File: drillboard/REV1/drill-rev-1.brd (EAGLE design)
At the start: 51.4 x 52.6 mm, 41 parts, among them M1 M03VERT, M2 M03VERT, M3 M03VERT, M4 M03VERT, T1 M03VERT, T2 M03VERT, T3 M03VERT, T4 M03VERT

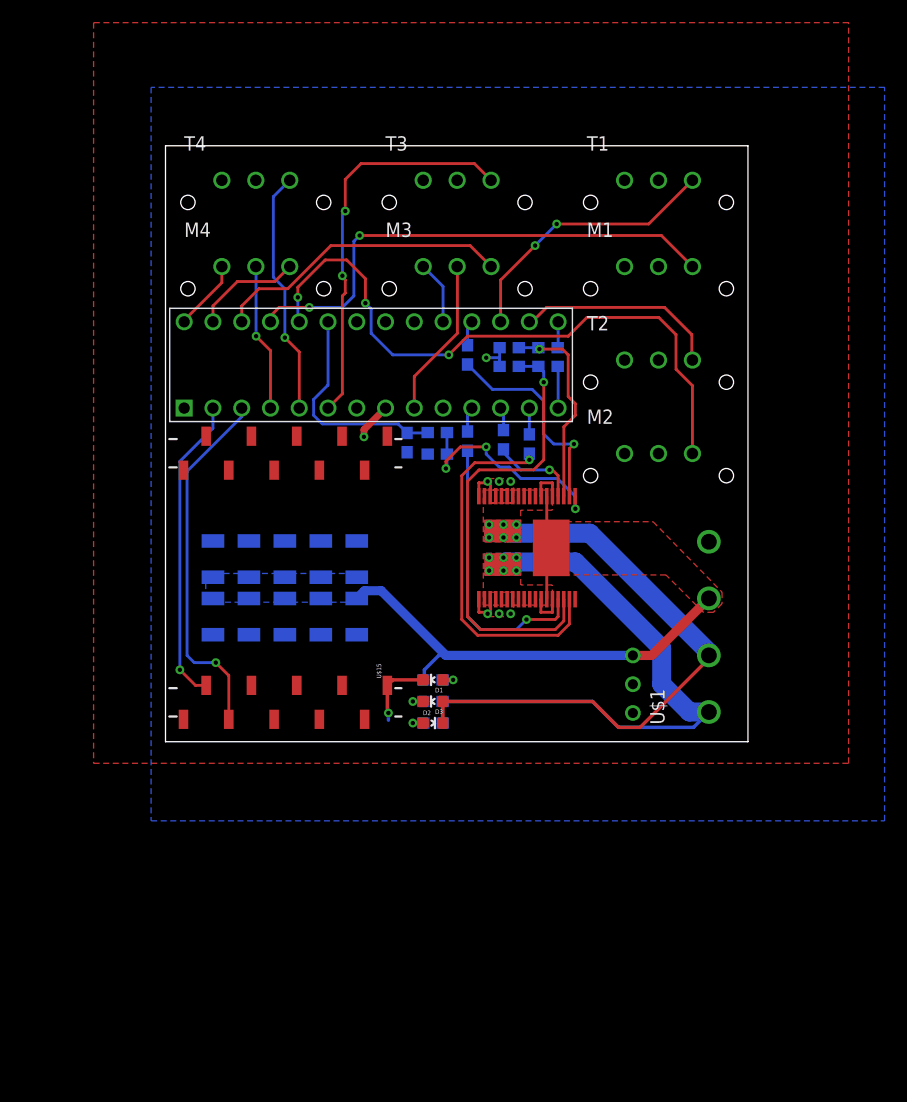
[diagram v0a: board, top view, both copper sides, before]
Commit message: regen gerbers and saved panelized brd file
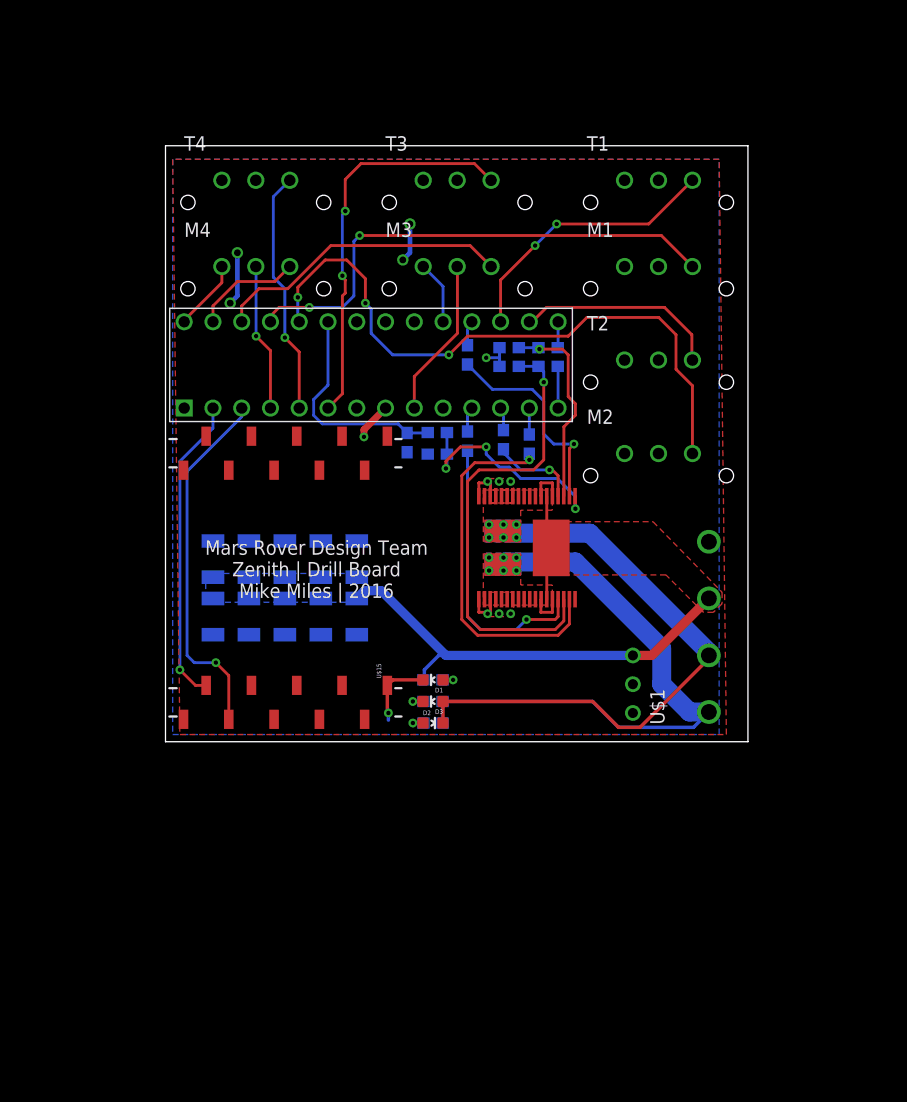
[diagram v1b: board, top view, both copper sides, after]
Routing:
- net +3V3: track 3.57 -> 11.7 mm, vias 1 -> 5
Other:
- board text added: "Mars Rover Design Team Zenith | Drill Board Mike Miles | 2016"
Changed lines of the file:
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@@
 <wire x1="51.435" y1="52.629" x2="0" y2="52.629" width="0" layer="20"/>
 <wire x1="0" y1="52.629" x2="0" y2="0" width="0" layer="20"/>
+<text x="13.335" y="12.7" size="1.27" layer="21" align="bottom-center">Mars Rover Design Team
+Zenith | Drill Board
+Mike Miles | 2016</text>
+<text x="13.335" y="12.7" size="1.27" layer="125" align="bottom-center">Mars Rover Design Team
+Zenith | Drill Board
+Mike Miles | 2016</text>
 </plain>
 <attributes>
@@
 <contactref element="C11" pad="2"/>
 <polygon width="0.4064" layer="16" rank="6">
-<vertex x="-1.27" y="57.785"/>
-<vertex x="-1.27" y="-6.985"/>
-<vertex x="63.5" y="-6.985"/>
-<vertex x="63.5" y="57.785"/>
+<vertex x="0.635" y="51.435"/>
+<vertex x="0.635" y="0.635"/>
+<vertex x="48.895" y="0.635"/>
+<vertex x="48.895" y="51.435"/>
 </polygon>
 <polygon width="0.254" layer="1" thermals="no">
@@
 <contactref element="U$15" pad="14"/>
 <polygon width="0.4064" layer="1" rank="6">
-<vertex x="-6.35" y="63.5"/>
-<vertex x="-6.35" y="-1.905"/>
-<vertex x="60.325" y="-1.905"/>
-<vertex x="60.325" y="63.5"/>
+<vertex x="0.635" y="51.435"/>
+<vertex x="1.27" y="0.635"/>
+<vertex x="49.53" y="0.635"/>
+<vertex x="48.895" y="51.435"/>
 </polygon>
 <wire x1="29.503" y1="34.798" x2="29.503" y2="33.147" width="0.254" layer="16"/>
@@
 <wire x1="29.464" y1="33.909" x2="28.321" y2="33.909" width="0.254" layer="16"/>
 <via x="28.321" y="33.909" extent="1-16" drill="0.381"/>
+<via x="5.715" y="38.735" extent="1-16" drill="0.6"/>
+<via x="6.35" y="43.18" extent="1-16" drill="0.6"/>
+<via x="20.955" y="42.545" extent="1-16" drill="0.6"/>
+<via x="21.59" y="45.72" extent="1-16" drill="0.6"/>
+<wire x1="5.715" y1="38.735" x2="6.35" y2="39.37" width="0.4064" layer="16"/>
+<wire x1="6.35" y1="39.37" x2="6.35" y2="43.18" width="0.4064" layer="16"/>
+<wire x1="20.955" y1="42.545" x2="21.59" y2="43.18" width="0.4064" layer="16"/>
+<wire x1="21.59" y1="43.18" x2="21.59" y2="45.72" width="0.4064" layer="16"/>
 </signal>
 <signal name="+12V">

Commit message: regen gerbers
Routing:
- net GND: track 16.5 -> 23.2 mm, vias 8 -> 10
- net OUTA: track 55.9 -> 58.9 mm
- net OUTB: track 54.6 -> 57.6 mm
- net +3V3: track 11.7 -> 13.7 mm
- net N$5: track 1.83 -> 2.59 mm
- net N$4: track 1.83 -> 2.59 mm
- net N$12: track 1.83 -> 2.59 mm
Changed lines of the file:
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@@
 <setting verticaltext="up"/>
 </settings>
-<grid distance="0.025" unitdist="inch" unit="inch" style="lines" multiple="1" display="yes" altdistance="0.005" altunitdist="inch" altunit="inch"/>
+<grid distance="0.005" unitdist="inch" unit="inch" style="lines" multiple="1" display="yes" altdistance="0.0005" altunitdist="inch" altunit="inch"/>
 <layers>
 <layer number="1" name="Top" color="4" fill="1" visible="yes" active="yes"/>
@@
 <plain>
 <wire x1="0" y1="0" x2="51.435" y2="0" width="0" layer="20"/>
-<wire x1="51.435" y1="0" x2="51.435" y2="52.629" width="0" layer="20"/>
-<wire x1="51.435" y1="52.629" x2="0" y2="52.629" width="0" layer="20"/>
-<wire x1="0" y1="52.629" x2="0" y2="0" width="0" layer="20"/>
+<wire x1="51.435" y1="0" x2="51.435" y2="52.6288" width="0" layer="20"/>
+<wire x1="51.435" y1="52.6288" x2="0" y2="52.6288" width="0" layer="20"/>
+<wire x1="0" y1="52.6288" x2="0" y2="0" width="0" layer="20"/>
 <text x="13.335" y="12.7" size="1.27" layer="21" align="bottom-center">Mars Rover Design Team
 Zenith | Drill Board
@@
 <contactref element="C10" pad="2"/>
 <contactref element="C11" pad="2"/>
-<polygon width="0.4064" layer="16" rank="6">
+<polygon width="0.4064" layer="16" isolate="0.254" rank="6">
 <vertex x="0.635" y="51.435"/>
 <vertex x="0.635" y="0.635"/>
@@
 <vertex x="48.895" y="51.435"/>
 </polygon>
-<polygon width="0.254" layer="1" thermals="no">
+<polygon width="0.254" layer="1" isolate="0.254" thermals="no">
 <vertex x="30.734" y="13.208"/>
 <vertex x="30.734" y="11.049"/>
@@
 <via x="29.464" y="11.303" extent="1-16" drill="0.381"/>
 <via x="30.48" y="11.303" extent="1-16" drill="0.381"/>
-<polygon width="0.254" layer="1" thermals="no">
+<polygon width="0.254" layer="1" isolate="0.254" thermals="no">
 <vertex x="30.734" y="21.082"/>
 <vertex x="30.734" y="23.241"/>
@@
 <wire x1="17.526" y1="26.924" x2="17.526" y2="27.559" width="0.6096" layer="1"/>
 <wire x1="17.526" y1="27.559" x2="19.431" y2="29.464" width="0.6096" layer="1"/>
+<wire x1="41.275" y1="5.08" x2="39.116" y2="5.08" width="0.6096" layer="16"/>
+<wire x1="39.116" y1="5.08" x2="37.973" y2="6.223" width="0.6096" layer="16"/>
+<via x="37.973" y="6.223" extent="1-16" drill="0.381"/>
+<wire x1="37.973" y1="6.223" x2="37.973" y2="9.144" width="0.6096" layer="1"/>
+<via x="37.973" y="9.144" extent="1-16" drill="0.381"/>
 </signal>
 <signal name="+3V3">
@@
 <contactref element="U$15" pad="1"/>
 <contactref element="U$15" pad="14"/>
-<polygon width="0.4064" layer="1" rank="6">
+<polygon width="0.4064" layer="1" isolate="0.254" rank="6">
 <vertex x="0.635" y="51.435"/>
 <vertex x="1.27" y="0.635"/>
@@
 <wire x1="20.955" y1="42.545" x2="21.59" y2="43.18" width="0.4064" layer="16"/>
 <wire x1="21.59" y1="43.18" x2="21.59" y2="45.72" width="0.4064" layer="16"/>
+<wire x1="1.59" y1="1.978" x2="3.556" y2="1.978" width="0.254" layer="1"/>
+<wire x1="3.556" y1="1.978" x2="3.556" y2="2.032" width="0.254" layer="1"/>
 </signal>
 <signal name="+12V">
@@
 <contactref element="U$13" pad="P$3"/>
 <contactref element="U$15" pad="3"/>
-<wire x1="5.59" y1="1.978" x2="5.59" y2="5.84" width="0.254" layer="1"/>
-<wire x1="5.59" y1="5.84" x2="4.445" y2="6.985" width="0.254" layer="1"/>
-<via x="4.445" y="6.985" extent="1-16" drill="0.381"/>
-<wire x1="4.445" y1="6.985" x2="2.54" y2="6.985" width="0.254" layer="16"/>
-<wire x1="2.54" y1="6.985" x2="1.905" y2="7.62" width="0.254" layer="16"/>
-<wire x1="1.905" y1="7.62" x2="1.905" y2="23.876" width="0.254" layer="16"/>
+<wire x1="5.59" y1="1.978" x2="5.59" y2="6.221" width="0.254" layer="1"/>
+<wire x1="5.59" y1="6.221" x2="4.445" y2="7.366" width="0.254" layer="1"/>
+<via x="4.445" y="7.366" extent="1-16" drill="0.381"/>
+<wire x1="4.445" y1="7.366" x2="2.54" y2="7.366" width="0.254" layer="16"/>
+<wire x1="2.54" y1="7.366" x2="1.905" y2="8.001" width="0.254" layer="16"/>
+<wire x1="1.905" y1="8.001" x2="1.905" y2="23.876" width="0.254" layer="16"/>
 <wire x1="1.905" y1="23.876" x2="6.731" y2="28.702" width="0.254" layer="16"/>
 <wire x1="6.731" y1="28.702" x2="6.731" y2="29.464" width="0.254" layer="16"/>
@@
 <contactref element="U$6" pad="P$9"/>
 <contactref element="U$6" pad="P$14"/>
-<polygon width="0.254" layer="1" thermals="no" rank="2">
+<polygon width="0.254" layer="1" isolate="0.254" thermals="no" rank="2">
 <vertex x="34.163" y="12.065"/>
 <vertex x="34.163" y="13.843"/>
@@
 <wire x1="40.005" y1="1.27" x2="46.628" y2="1.27" width="0.3048" layer="16"/>
 <wire x1="46.628" y1="1.27" x2="47.985" y2="2.627" width="0.3048" layer="16"/>
+<wire x1="28.17" y1="12.585" x2="28.1686" y2="12.585" width="0.254" layer="1"/>
+<wire x1="28.1686" y1="12.585" x2="28.1686" y2="14.351" width="0.254" layer="1"/>
+<wire x1="28.1686" y1="14.351" x2="28.575" y2="14.351" width="0.254" layer="1"/>
+<wire x1="28.575" y1="14.351" x2="28.575" y2="15.113" width="0.254" layer="1"/>
 </signal>
 <signal name="OUTB">
@@
 <contactref element="U$6" pad="P$23"/>
 <contactref element="U$6" pad="P$28"/>
-<polygon width="0.254" layer="1" thermals="no">
+<polygon width="0.254" layer="1" isolate="0.254" thermals="no">
 <vertex x="34.163" y="22.225"/>
 <vertex x="34.163" y="20.447"/>
@@
 <wire x1="41.91" y1="1.27" x2="47.985" y2="7.345" width="0.3048" layer="1"/>
 <wire x1="47.985" y1="7.345" x2="47.985" y2="7.627" width="0.3048" layer="1"/>
+<wire x1="28.17" y1="21.685" x2="28.1686" y2="21.685" width="0.254" layer="1"/>
+<wire x1="28.1686" y1="21.685" x2="28.1686" y2="19.7993" width="0.254" layer="1"/>
+<wire x1="28.1686" y1="19.7993" x2="28.575" y2="19.7993" width="0.254" layer="1"/>
+<wire x1="28.575" y1="19.7993" x2="28.575" y2="19.177" width="0.254" layer="1"/>
 </signal>
 <signal name="CS">
@@
 <contactref element="R1" pad="2"/>
 <contactref element="D1" pad="A"/>
-<wire x1="24.499" y1="5.461" x2="25.4" y2="5.461" width="0.254" layer="1"/>
-<via x="25.4" y="5.461" extent="1-16" drill="0.381"/>
-<wire x1="25.4" y1="5.461" x2="24.472" y2="5.461" width="0.254" layer="16"/>
+<wire x1="24.499" y1="5.461" x2="25.781" y2="5.461" width="0.254" layer="1"/>
+<via x="25.781" y="5.461" extent="1-16" drill="0.381"/>
+<wire x1="25.781" y1="5.461" x2="24.472" y2="5.461" width="0.254" layer="16"/>
 </signal>
 <signal name="N$5">
 <contactref element="R12" pad="2"/>
 <contactref element="D2" pad="A"/>
-<wire x1="22.772" y1="1.651" x2="21.844" y2="1.651" width="0.254" layer="16"/>
-<via x="21.844" y="1.651" extent="1-16" drill="0.381"/>
-<wire x1="21.844" y1="1.651" x2="22.745" y2="1.651" width="0.254" layer="1"/>
+<wire x1="22.772" y1="1.651" x2="21.463" y2="1.651" width="0.254" layer="16"/>
+<via x="21.463" y="1.651" extent="1-16" drill="0.381"/>
+<wire x1="21.463" y1="1.651" x2="22.745" y2="1.651" width="0.254" layer="1"/>
 </signal>
 <signal name="N$12">
 <contactref element="D3" pad="C"/>
 <contactref element="R13" pad="2"/>
-<wire x1="22.772" y1="3.556" x2="21.844" y2="3.556" width="0.254" layer="16"/>
-<via x="21.844" y="3.556" extent="1-16" drill="0.381"/>
-<wire x1="21.844" y1="3.556" x2="22.745" y2="3.556" width="0.254" layer="1"/>
+<wire x1="22.772" y1="3.556" x2="21.463" y2="3.556" width="0.254" layer="16"/>
+<via x="21.463" y="3.556" extent="1-16" drill="0.381"/>
+<wire x1="21.463" y1="3.556" x2="22.745" y2="3.556" width="0.254" layer="1"/>
 </signal>
 </signals>

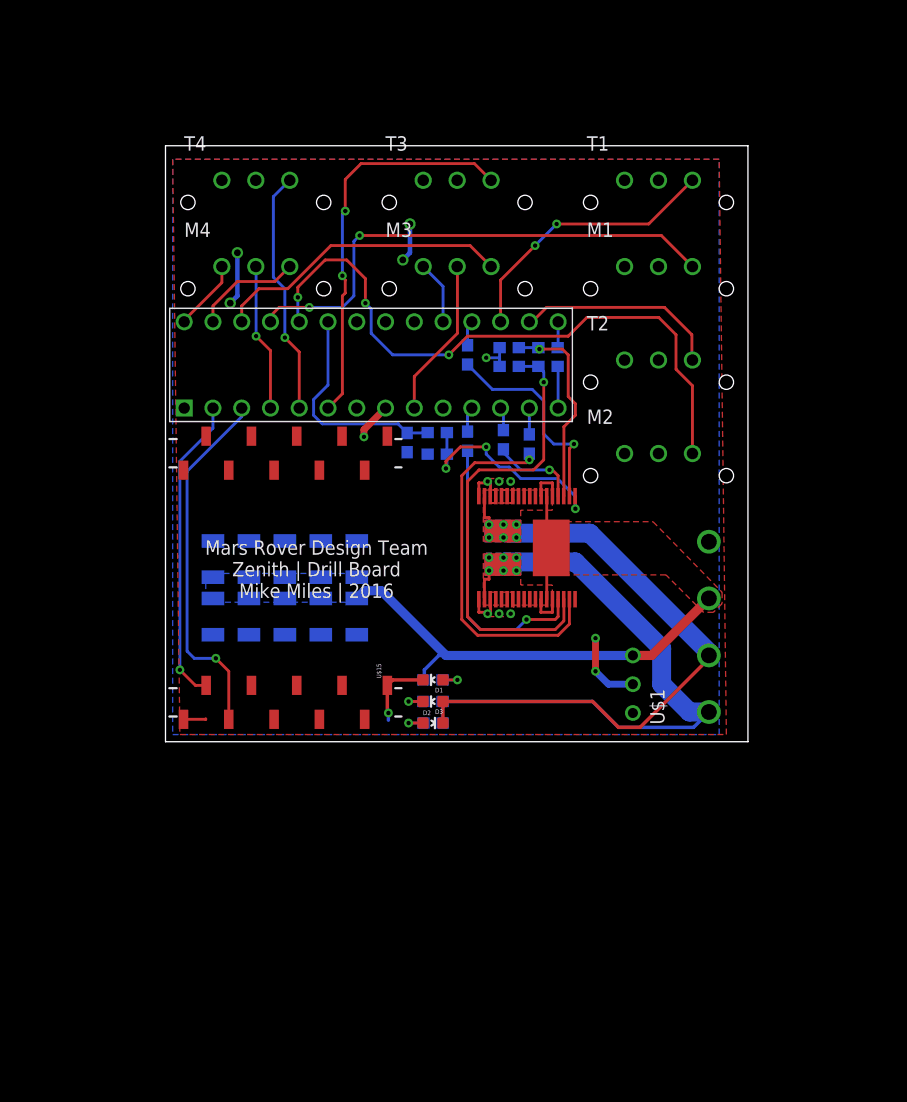
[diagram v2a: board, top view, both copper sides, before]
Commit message: made modifications for testing
- moved pwm to PD6
- moved INB to PB5
- removed custom moisture sensor M3
- added crystal oscillator to ATMEGA328p
- added resistors to make moisture sensor M4 work
NOTE: These changes were added post-production and were not actually
incorporated in the REV3 board. Disregard board design, schematic
changed for reference only.
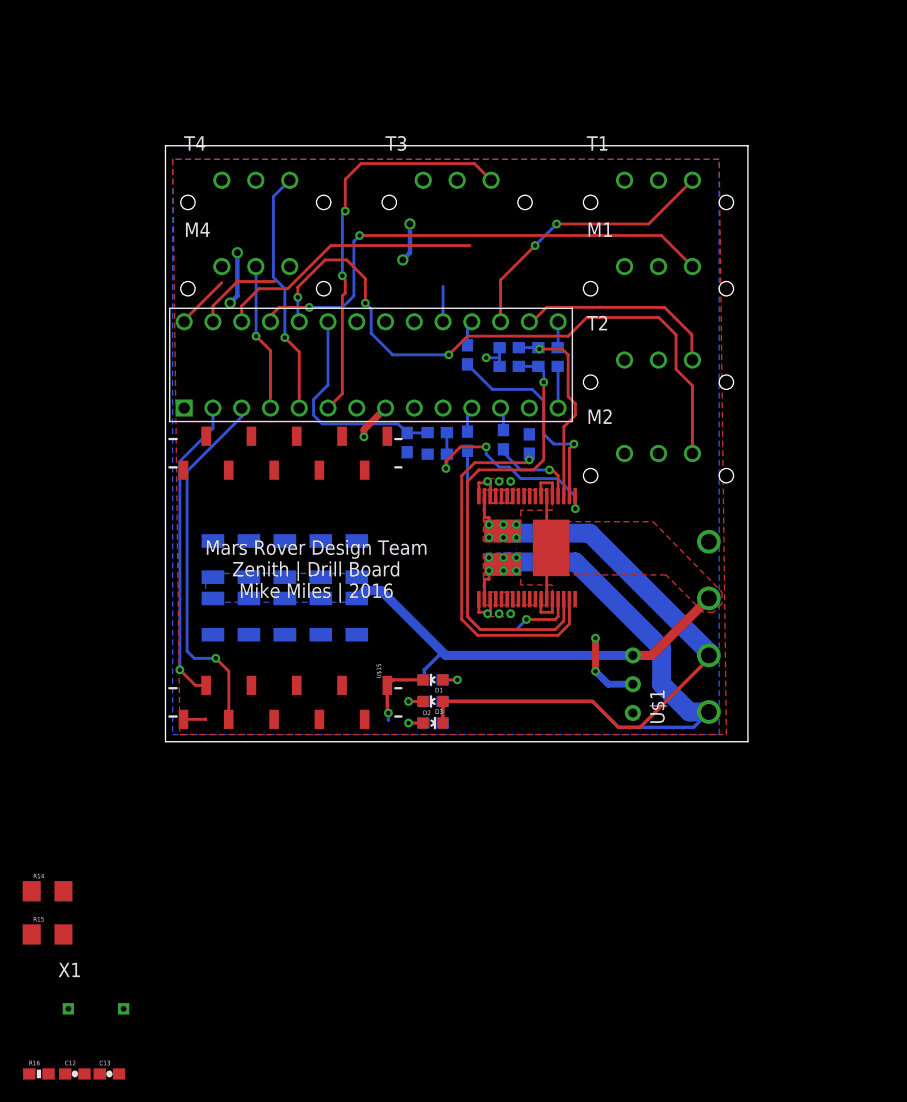
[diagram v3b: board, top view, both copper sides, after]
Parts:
- removed M3: M03VERT, MRDT-Connectors:MOLEX0436500328
- added C12, C13: 22p, SparkFun-Passives:0603-CAP
- added R14: 100, SparkFun-Resistors:1206
- added R15: 60, SparkFun-Resistors:1206
- added R16: 1M, SparkFun-Resistors:0603-RES
- added X1: X_HC49SCRYSTAL, MRDT-2014-All:HC-49
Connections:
- removed net D1: M3.P$3, U$13.P$19
- removed net D2: M3.P$2, U$13.P$9
- new net N$1: M4.P$3, R14.2
- new net XTAL1: C12.2, R16.1, U$13.P$9, X1.P$2
- new net XTAL2: C13.2, R16.2, U$13.P$10, X1.P$1
- net D3: now also R14.1; no longer M4.P$3
- net D4: now also R15.2; no longer M4.P$2
- net GND: now also C12.1, C13.1
- net INB: now also U$13.P$19; no longer U$13.P$12
- net MOIST_3: no longer M3.P$1
- net MOIST_4: now also M4.P$2, R15.1; no longer M4.P$1
- net PWM: now also U$13.P$12; no longer U$13.P$13
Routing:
- net D2: track 14.1 -> 0.00 mm
- net D1: track 5.60 -> 0.00 mm
- net INB: track 2.05 -> 4.81 mm
- net MOIST_3: track 26.4 -> 23.8 mm
- net PWM: track 2.32 -> 0.00 mm
- net MOIST_4: track 9.62 -> 7.75 mm
- net D3: track 6.26 -> 4.83 mm

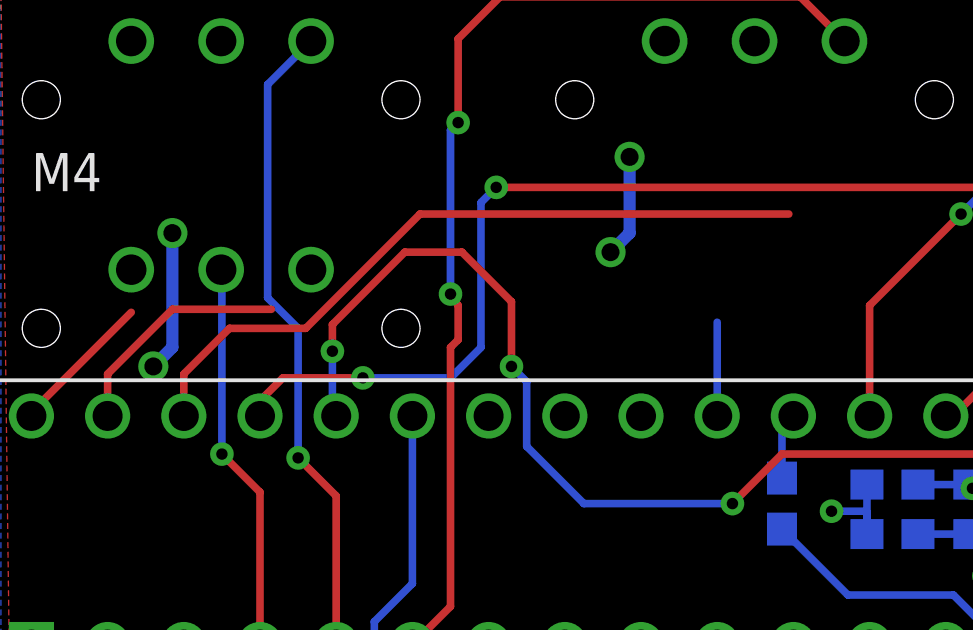
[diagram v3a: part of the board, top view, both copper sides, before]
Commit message: removed MOIST_3 net from sch
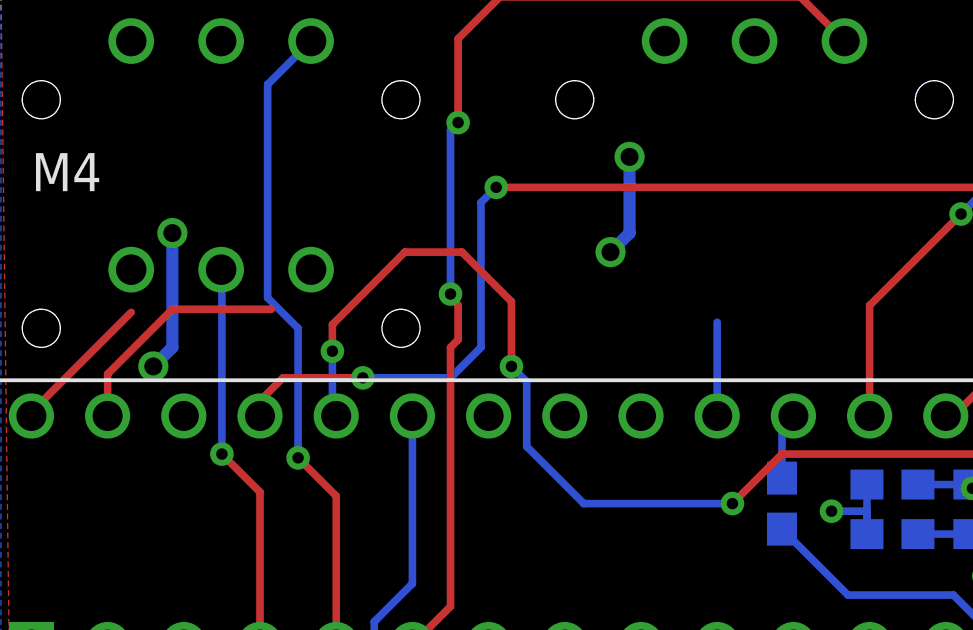
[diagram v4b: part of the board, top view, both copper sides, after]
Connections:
- removed net MOIST_3: U$13.P$26
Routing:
- net MOIST_3: track 23.8 -> 0.00 mm
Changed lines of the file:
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@@
 <wire x1="11.684" y1="39.243" x2="11.684" y2="40.132" width="0.254" layer="1"/>
-</signal>
-<signal name="MOIST_3">
-<contactref element="U$13" pad="P$26"/>
-<wire x1="6.731" y1="37.084" x2="6.731" y2="38.481" width="0.254" layer="1"/>
-<wire x1="6.731" y1="38.481" x2="8.255" y2="40.005" width="0.254" layer="1"/>
-<wire x1="8.255" y1="40.005" x2="10.795" y2="40.005" width="0.254" layer="1"/>
-<wire x1="10.795" y1="40.005" x2="14.605" y2="43.815" width="0.254" layer="1"/>
-<wire x1="14.605" y1="43.815" x2="26.8986" y2="43.815" width="0.254" layer="1"/>
 </signal>
 <signal name="MOIST_4">
